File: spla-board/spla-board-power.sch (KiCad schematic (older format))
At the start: 41 parts, among them J12 J_POWER, J4 J_POWER2, J7 Barrel_Jack, U14 TLV73311PDBV, U7 ST1S10PHR, U8 ST1S10PHR, U9 TLV73325PDBV

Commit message: schematic/pcb: Add LEDs for FPGA status signals; rework layout to suit.
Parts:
- R86: value 150 -> 750
- R96: value 68 -> 330
- renumbered D3 to D1, D5 to D2
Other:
- note added: "(3.3V - 2.0V) / 4mA = 325 ohm"
- note added: "(5.0V - 2.0V) / 4mA = 750 ohm"
- note removed: "(3.3V - 2.0V) / 20mA = 65 ohm"
- note removed: "(5.0V - 2.0V) / 20mA = 150 ohm"
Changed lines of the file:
@@
 P 9350 3600
 AR Path="/5E4F712F/5EB36971" Ref="D?"  Part="1"
-AR Path="/5E50D39B/5EB36971" Ref="D5"  Part="1"
-F 0 "D5" V 9389 3483 50  0000 R CNN
+AR Path="/5E50D39B/5EB36971" Ref="D2"  Part="1"
+F 0 "D2" V 9389 3483 50  0000 R CNN
 F 1 "LED" V 9298 3483 50  0000 R CNN
 F 2 "LED_SMD:LED_0805_2012Metric" H 9350 3600 50  0001 C CNN
@@
 AR Path="/5E50D39B/5EB36977" Ref="R86"  Part="1"
 F 0 "R86" H 9409 3996 50  0000 L CNN
-F 1 "150" H 9409 3905 50  0000 L CNN
+F 1 "750" H 9409 3905 50  0000 L CNN
 F 2 "Resistor_SMD:R_0603_1608Metric" H 9350 3950 50  0001 C CNN
 F 3 "~" H 9350 3950 50  0001 C CNN
@@
 $EndComp
 Text Notes 8350 4550 0    50   ~ 0
-(5.0V - 2.0V) / 20mA = 150 ohm
+(5.0V - 2.0V) / 4mA = 750 ohm
 Wire Wire Line
 	9350 3350 9350 3450
@@
 P 9350 5650
 AR Path="/5E4F712F/5EB3D482" Ref="D?"  Part="1"
-AR Path="/5E50D39B/5EB3D482" Ref="D3"  Part="1"
-F 0 "D3" V 9389 5533 50  0000 R CNN
+AR Path="/5E50D39B/5EB3D482" Ref="D1"  Part="1"
+F 0 "D1" V 9389 5533 50  0000 R CNN
 F 1 "LED" V 9298 5533 50  0000 R CNN
 F 2 "LED_SMD:LED_0805_2012Metric" H 9350 5650 50  0001 C CNN
@@
 AR Path="/5E50D39B/5EB3D48C" Ref="R96"  Part="1"
 F 0 "R96" H 9409 6046 50  0000 L CNN
-F 1 "68" H 9409 5955 50  0000 L CNN
+F 1 "330" H 9409 5955 50  0000 L CNN
 F 2 "Resistor_SMD:R_0603_1608Metric" H 9350 6000 50  0001 C CNN
 F 3 "~" H 9350 6000 50  0001 C CNN
@@
 $EndComp
 Text Notes 8350 6600 0    50   ~ 0
-(3.3V - 2.0V) / 20mA = 65 ohm
+(3.3V - 2.0V) / 4mA = 325 ohm
 Wire Wire Line
 	9350 5400 9350 5500

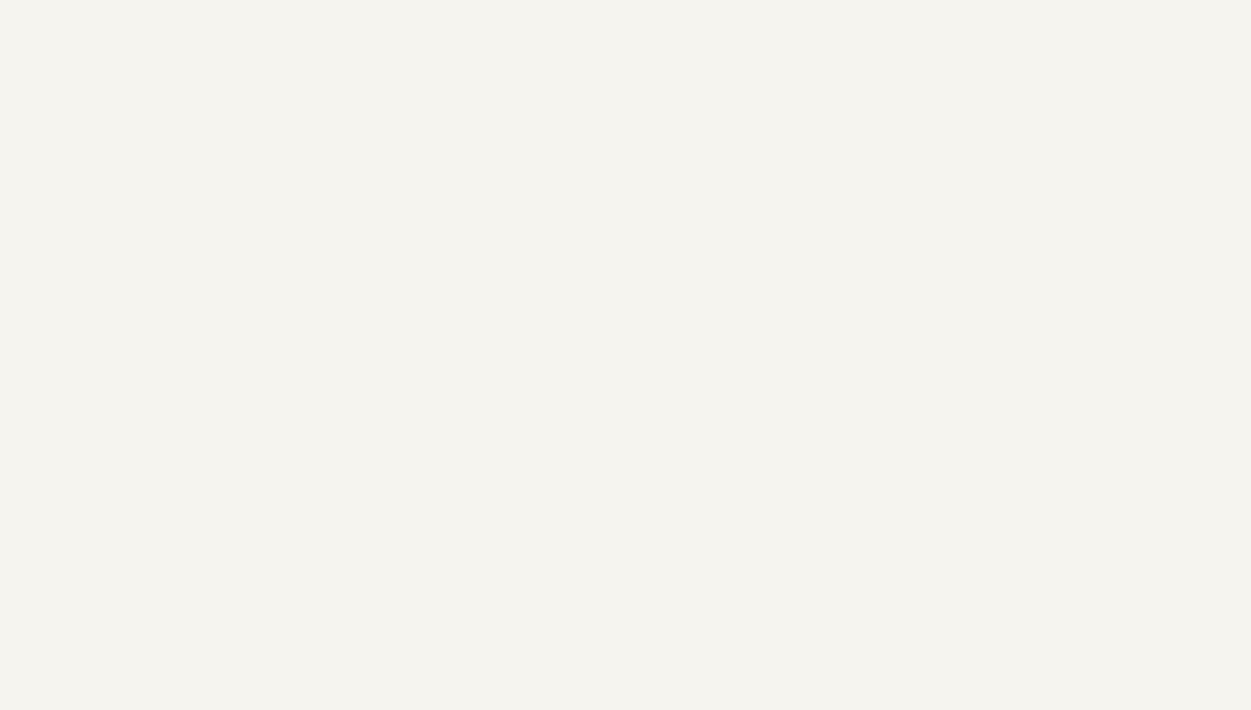
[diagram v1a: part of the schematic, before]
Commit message: schematic/pcb: Give up on remaining FPGA decoupling; Add distributed decoupling to hopefully mitigate.
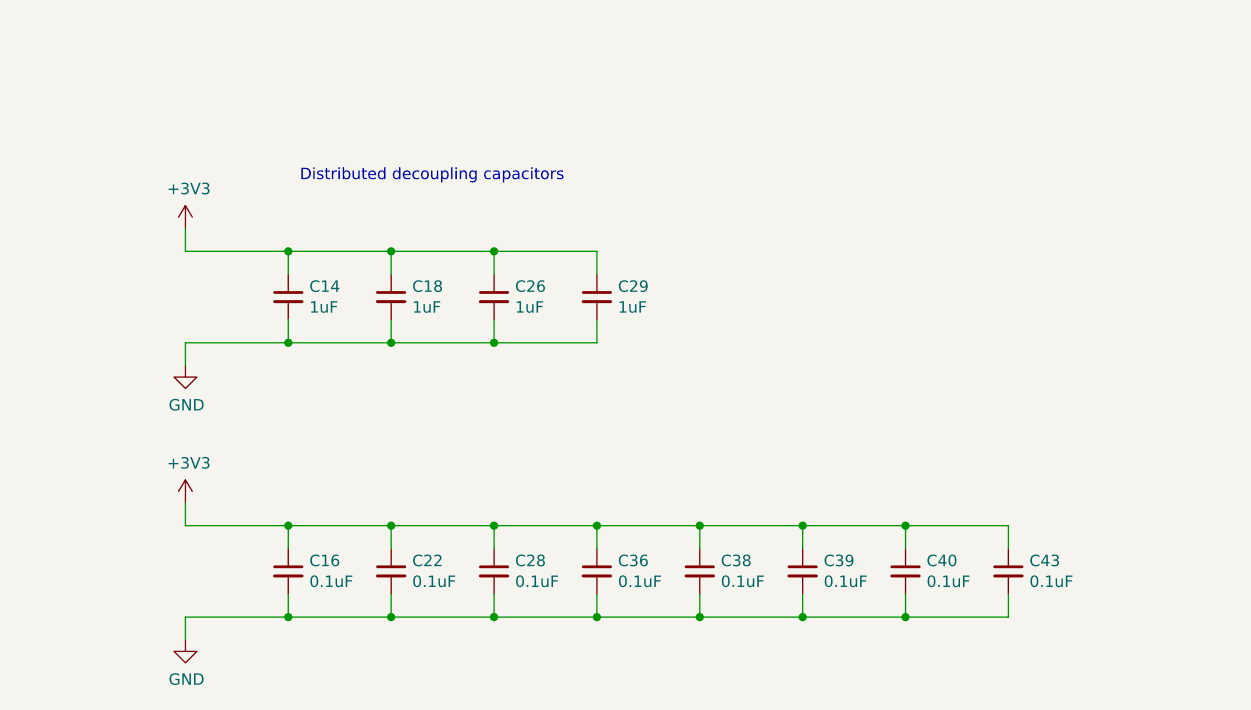
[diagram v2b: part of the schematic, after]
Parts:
- added C14, C18, C26, C29: 1uF, Capacitor_SMD:C_0603_1608Metric, symbol Device:C_Small
- added C16, C22, C28, C36, C38, C39, C40, C43: 0.1uF, Capacitor_SMD:C_0603_1608Metric, symbol Device:C_Small
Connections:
- net +3V3: now also C14.1, C16.1, C18.1, C22.1, C26.1, C28.1, C29.1, C36.1, C38.1, C39.1, C40.1, C43.1
- net GND: now also C14.2, C16.2, C18.2, C22.2, C26.2, C28.2, C29.2, C36.2, C38.2, C39.2, C40.2, C43.2
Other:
- note added: "Distributed decoupling capacitors"

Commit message: schematic: Add Digikey and ManufacturerId fields to big components.
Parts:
- L1, L2: Digikey (none) -> 541-1237-1-ND; Manufacturer Id (none) -> IHLP2020CZER3R3M11
- U14: Digikey (none) -> 296-40663-1-ND; Manufacturer Id (none) -> TLV73311PDBVR
- U7, U8: Digikey (none) -> 497-6904-1-ND; Manufacturer Id (none) -> ST1S10PHR
- U9: Digikey (none) -> 296-40671-1-ND; Manufacturer Id (none) -> TLV73325PDBVR
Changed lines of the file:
@@
 F 2 "SPLA:ST_PowerSO-8EP_4x5mm_P1.27mm_EP3.5x2.6mm" H 6000 3100 50  0001 C CNN
 F 3 "" H 6000 3800 50  0001 C CNN
+F 4 "497-6904-1-ND" H 6000 3750 50  0001 C CNN "Digikey"
+F 5 "ST1S10PHR" H 6000 3750 50  0001 C CNN "Manufacturer Id"
 	1    6000 3750
 	1    0    0    -1
@@
 F 2 "SPLA:ST_PowerSO-8EP_4x5mm_P1.27mm_EP3.5x2.6mm" H 6000 5150 50  0001 C CNN
 F 3 "" H 6000 5850 50  0001 C CNN
+F 4 "497-6904-1-ND" H 6000 5800 50  0001 C CNN "Digikey"
+F 5 "ST1S10PHR" H 6000 5800 50  0001 C CNN "Manufacturer Id"
 	1    6000 5800
 	1    0    0    -1
@@
 F 2 "Inductor_SMD:L_Vishay_IHLP-2020" H 6700 3350 50  0001 C CNN
 F 3 "~" H 6700 3350 50  0001 C CNN
+F 4 "541-1237-1-ND" H 6700 3350 50  0001 C CNN "Digikey"
+F 5 "IHLP2020CZER3R3M11" H 6700 3350 50  0001 C CNN "Manufacturer Id"
 	1    6700 3350
 	0    -1   -1   0
@@
 F 2 "Inductor_SMD:L_Vishay_IHLP-2020" H 6700 5400 50  0001 C CNN
 F 3 "~" H 6700 5400 50  0001 C CNN
+F 4 "541-1237-1-ND" H 6700 5400 50  0001 C CNN "Digikey"
+F 5 "IHLP2020CZER3R3M11" H 6700 5400 50  0001 C CNN "Manufacturer Id"
 	1    6700 5400
 	0    -1   -1   0
@@
 F 2 "Package_TO_SOT_SMD:SOT-23-5" H 13200 6775 50  0001 C CIN
 F 3 "http://www.ti.com/lit/ds/symlink/tlv733p.pdf" H 13200 6450 50  0001 C CNN
+F 4 "296-40663-1-ND" H 13200 6450 50  0001 C CNN "Digikey"
+F 5 "TLV73311PDBVR" H 13200 6450 50  0001 C CNN "Manufacturer Id"
 	1    13200 6450
 	1    0    0    -1
@@
 F 2 "Package_TO_SOT_SMD:SOT-23-5" H 13200 5525 50  0001 C CIN
 F 3 "http://www.ti.com/lit/ds/symlink/tlv733p.pdf" H 13200 5200 50  0001 C CNN
+F 4 "296-40671-1-ND" H 13200 5200 50  0001 C CNN "Digikey"
+F 5 "TLV73325PDBVR" H 13200 5200 50  0001 C CNN "Manufacturer Id"
 	1    13200 5200
 	1    0    0    -1

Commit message: schematic: Select LED part.
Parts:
- D1, D2: Digikey (none) -> 732-4986-1-ND; Manufacturer Id (none) -> 150080VS75000
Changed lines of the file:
@@
 F 2 "LED_SMD:LED_0805_2012Metric" H 9350 3600 50  0001 C CNN
 F 3 "~" H 9350 3600 50  0001 C CNN
+F 4 "732-4986-1-ND" H 9350 3600 50  0001 C CNN "Digikey"
+F 5 "150080VS75000" H 9350 3600 50  0001 C CNN "Manufacturer Id"
 	1    9350 3600
 	0    -1   -1   0
@@
 F 2 "LED_SMD:LED_0805_2012Metric" H 9350 5650 50  0001 C CNN
 F 3 "~" H 9350 5650 50  0001 C CNN
+F 4 "732-4986-1-ND" H 9350 5650 50  0001 C CNN "Digikey"
+F 5 "150080VS75000" H 9350 5650 50  0001 C CNN "Manufacturer Id"
 	1    9350 5650
 	0    -1   -1   0

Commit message: schematic: Add part numbers for USB and power jack.
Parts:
- J7: Digikey (none) -> CP-036AHPJCT-ND; Manufacturer Id (none) -> PJ-036AH-SMT-TR
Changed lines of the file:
@@
 F 2 "Connector_BarrelJack:BarrelJack_CUI_PJ-036AH-SMT_Horizontal" H 1100 3410 50  0001 C CNN
 F 3 "~" H 1100 3410 50  0001 C CNN
+F 4 "CP-036AHPJCT-ND" H 1050 3450 50  0001 C CNN "Digikey"
+F 5 "PJ-036AH-SMT-TR" H 1050 3450 50  0001 C CNN "Manufacturer Id"
 	1    1050 3450
 	1    0    0    -1

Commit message: schematic: Set 'N/A' for test points and holes 'parts'.
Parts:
- H1, H2, H3, H4, TP5, TP6: Digikey (none) -> N/A; Manufacturer Id (none) -> N/A
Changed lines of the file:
@@
 F 2 "TestPoint:TestPoint_Pad_D2.0mm" H 2700 3250 50  0001 C CNN
 F 3 "~" H 2700 3250 50  0001 C CNN
+F 4 "N/A" H 2500 3250 50  0001 C CNN "Digikey"
+F 5 "N/A" H 2500 3250 50  0001 C CNN "Manufacturer Id"
 	1    2500 3250
 	1    0    0    -1
@@
 F 2 "MountingHole:MountingHole_3.2mm_M3_Pad" H 13400 8150 50  0001 C CNN
 F 3 "~" H 13400 8150 50  0001 C CNN
+F 4 "N/A" H 13400 8150 50  0001 C CNN "Digikey"
+F 5 "N/A" H 13400 8150 50  0001 C CNN "Manufacturer Id"
 	1    13400 8150
 	1    0    0    -1
@@
 F 2 "MountingHole:MountingHole_3.2mm_M3_Pad" H 14400 8150 50  0001 C CNN
 F 3 "~" H 14400 8150 50  0001 C CNN
+F 4 "N/A" H 14400 8150 50  0001 C CNN "Digikey"
+F 5 "N/A" H 14400 8150 50  0001 C CNN "Manufacturer Id"
 	1    14400 8150
 	1    0    0    -1
@@
 F 2 "MountingHole:MountingHole_3.2mm_M3_Pad" H 13400 8650 50  0001 C CNN
 F 3 "~" H 13400 8650 50  0001 C CNN
+F 4 "N/A" H 13400 8650 50  0001 C CNN "Digikey"
+F 5 "N/A" H 13400 8650 50  0001 C CNN "Manufacturer Id"
 	1    13400 8650
 	1    0    0    -1
@@
 F 2 "MountingHole:MountingHole_3.2mm_M3_Pad" H 14400 8650 50  0001 C CNN
 F 3 "~" H 14400 8650 50  0001 C CNN
+F 4 "N/A" H 14400 8650 50  0001 C CNN "Digikey"
+F 5 "N/A" H 14400 8650 50  0001 C CNN "Manufacturer Id"
 	1    14400 8650
 	1    0    0    -1
@@
 F 2 "TestPoint:TestPoint_Pad_D2.0mm" H 2700 3650 50  0001 C CNN
 F 3 "~" H 2700 3650 50  0001 C CNN
+F 4 "N/A" H 2500 3650 50  0001 C CNN "Digikey"
+F 5 "N/A" H 2500 3650 50  0001 C CNN "Manufacturer Id"
 	1    2500 3650
 	1    0    0    -1

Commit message: schematic: Add part numbers for pinheaders (albeit that these are breakaways, and it's not one-per-part).
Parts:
- J12, J4: Digikey (none) -> S2011EC-40-ND; Manufacturer Id (none) -> PRPC040DAAN-RC
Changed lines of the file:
@@
 F 2 "Connector_PinHeader_2.54mm:PinHeader_2x08_P2.54mm_Vertical" H 10750 4700 50  0001 C CNN
 F 3 "~" H 10750 4700 50  0001 C CNN
+F 4 "S2011EC-40-ND" H 10750 4700 50  0001 C CNN "Digikey"
+F 5 "PRPC040DAAN-RC" H 10750 4700 50  0001 C CNN "Manufacturer Id"
 	1    10750 4700
 	-1   0    0    -1
@@
 F 2 "Connector_PinHeader_2.54mm:PinHeader_2x02_P2.54mm_Vertical" H 14600 5950 50  0001 C CNN
 F 3 "~" H 14600 5950 50  0001 C CNN
+F 4 "S2011EC-40-ND" H 14600 5950 50  0001 C CNN "Digikey"
+F 5 "PRPC040DAAN-RC" H 14600 5950 50  0001 C CNN "Manufacturer Id"
 	1    14600 5950
 	1    0    0    1
